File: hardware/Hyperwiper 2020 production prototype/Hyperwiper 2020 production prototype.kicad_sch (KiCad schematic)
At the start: 28 parts, among them J1 Conn_01x05, K1 Main Power relay, K2 Wiper control relay, Q1 PN2222A, Q2 IRF540N, SW1 ON-OFF, SW2 SW_Reed, U1 Teensy4.0, U3 Voltage regulator

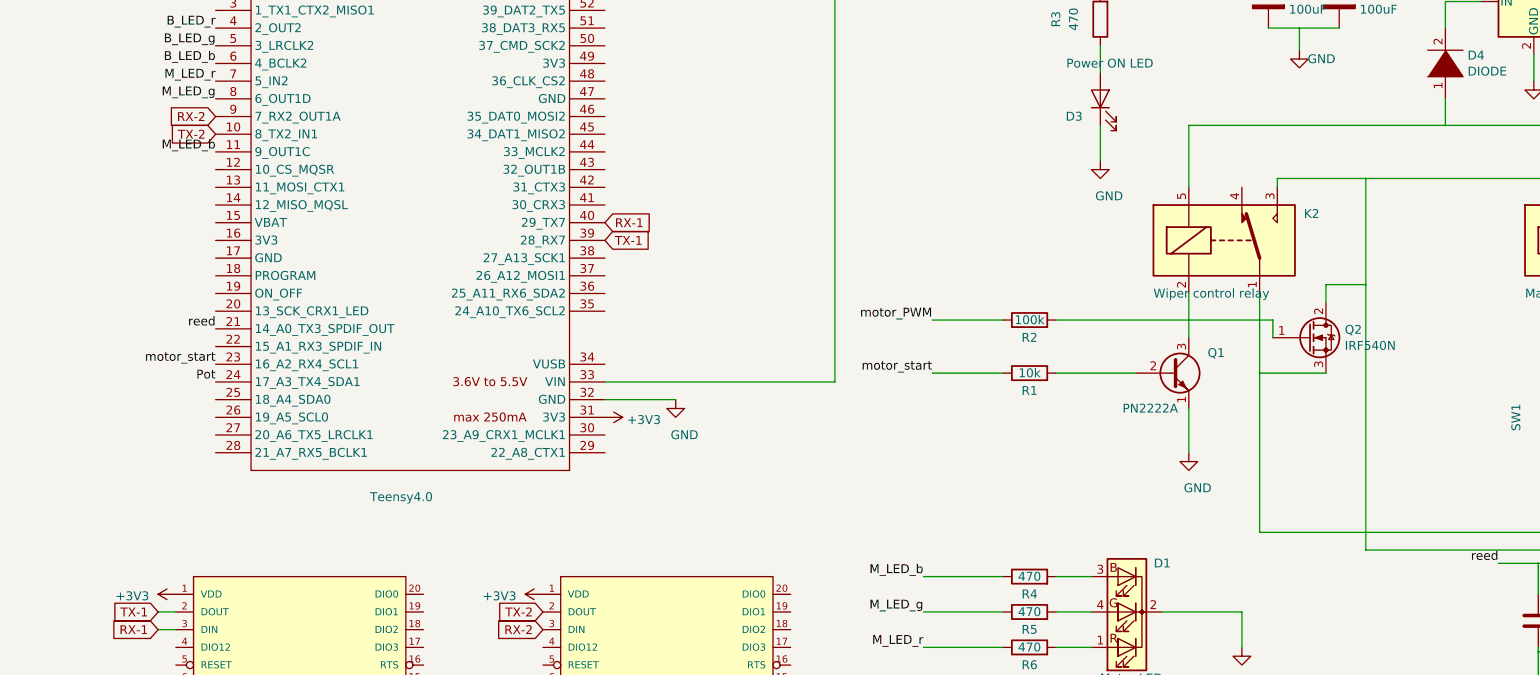
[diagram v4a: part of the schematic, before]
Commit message: Updated schematic for MOSFET
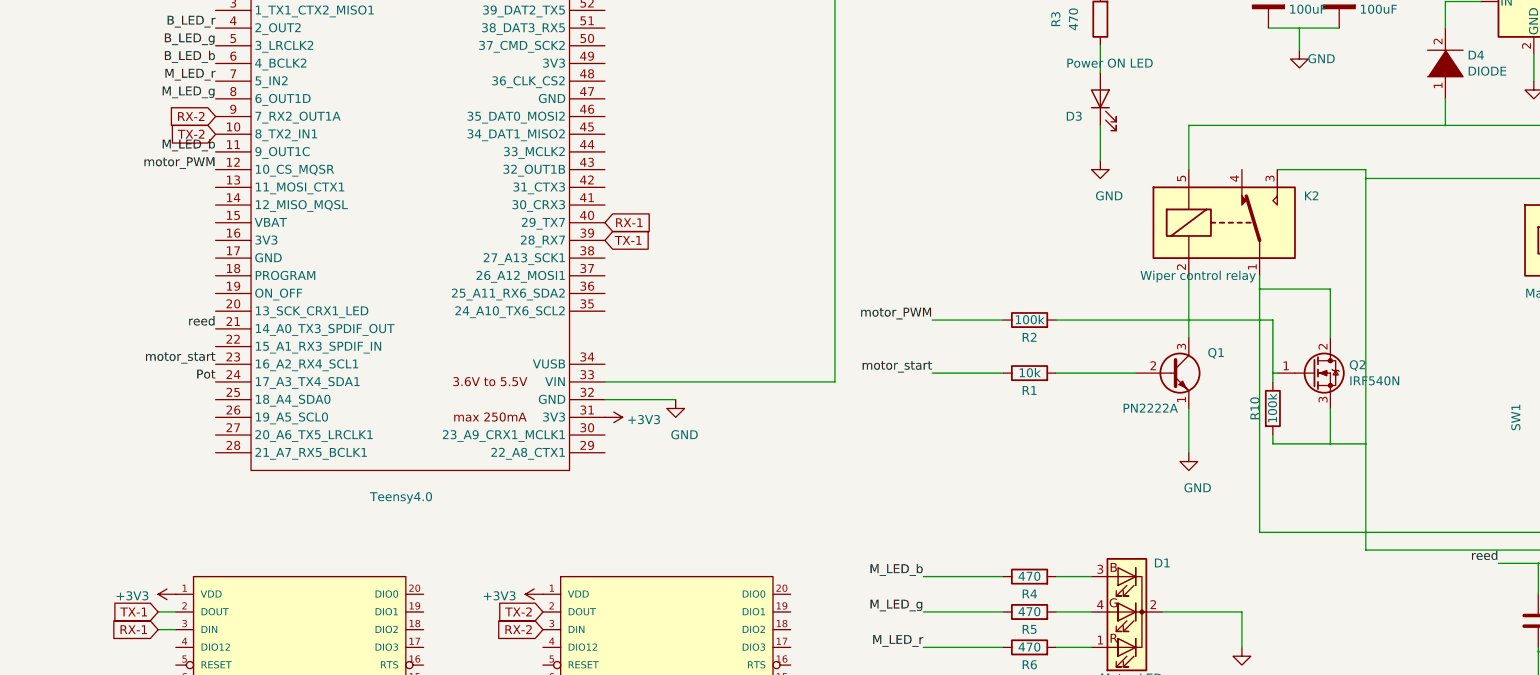
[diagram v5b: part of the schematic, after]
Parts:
- added R10: 100k, Resistor_THT:R_Axial_DIN0207_L6.3mm_D2.5mm_P10.16mm_Horizontal, symbol Device:R
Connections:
- net motor_PWM: now also U1.12 (10_CS_MQSR)
- net at Q2.1 (G), R2.2: now also R10.1
- net at J1.1 (Pin_1), K1.1, K1.5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: now also Q2.2 (D); no longer Q2.3 (S)
- net at J1.2 (Pin_2), K1.4, K2.3: now also Q2.3 (S), R10.2; no longer Q2.2 (D)
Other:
- moved on the sheet: K2, Q2
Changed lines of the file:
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@@
   )
   (junction (at 179.07 20.32) (diameter 0.259) (color 0 0 0 0))
-  (junction (at 201.93 82.55) (diameter 0.259) (color 0 0 0 0))
+  (junction (at 201.93 70.485) (diameter 0.259) (color 0 0 0 0))
+  (junction (at 203.835 82.55) (diameter 0.259) (color 0 0 0 0))
   (junction (at 207.645 33.02) (diameter 0.259) (color 0 0 0 0))
+  (junction (at 212.09 92.71) (diameter 0.259) (color 0 0 0 0))
   (junction (at 213.36 20.32) (diameter 0.259) (color 0 0 0 0))
   (junction (at 217.17 54.61) (diameter 0.259) (color 0 0 0 0))
-  (junction (at 217.17 69.85) (diameter 0.259) (color 0 0 0 0))
+  (junction (at 217.17 92.71) (diameter 0.259) (color 0 0 0 0))
   (junction (at 228.6 46.99) (diameter 0.259) (color 0 0 0 0))
   (junction (at 241.935 109.855) (diameter 0.259) (color 0 0 0 0))
@@
     (stroke (width 0) (type solid) (color 0 0 0 0))
   )
-  (wire (pts (xy 191.77 55.88) (xy 191.77 46.99))
-    (stroke (width 0) (type solid) (color 0 0 0 0))
-  )
-  (wire (pts (xy 191.77 71.12) (xy 191.77 77.47))
+  (wire (pts (xy 191.77 53.34) (xy 191.77 46.99))
+    (stroke (width 0) (type solid) (color 0 0 0 0))
+  )
+  (wire (pts (xy 191.77 68.58) (xy 191.77 77.47))
     (stroke (width 0) (type solid) (color 0 0 0 0))
   )
@@
     (stroke (width 0) (type solid) (color 0 0 0 0))
   )
-  (wire (pts (xy 201.93 71.12) (xy 201.93 82.55))
-    (stroke (width 0) (type solid) (color 0 0 0 0))
-  )
-  (wire (pts (xy 201.93 82.55) (xy 201.93 105.41))
-    (stroke (width 0) (type solid) (color 0 0 0 0))
-  )
-  (wire (pts (xy 201.93 82.55) (xy 211.455 82.55))
+  (wire (pts (xy 201.93 68.58) (xy 201.93 70.485))
+    (stroke (width 0) (type solid) (color 0 0 0 0))
+  )
+  (wire (pts (xy 201.93 70.485) (xy 201.93 105.41))
+    (stroke (width 0) (type solid) (color 0 0 0 0))
+  )
+  (wire (pts (xy 201.93 70.485) (xy 212.09 70.485))
     (stroke (width 0) (type solid) (color 0 0 0 0))
   )
@@
     (stroke (width 0) (type solid) (color 0 0 0 0))
   )
-  (wire (pts (xy 203.835 74.93) (xy 203.835 77.47))
-    (stroke (width 0) (type solid) (color 0 0 0 0))
-  )
-  (wire (pts (xy 204.47 54.61) (xy 217.17 54.61))
-    (stroke (width 0) (type solid) (color 0 0 0 0))
-  )
-  (wire (pts (xy 204.47 55.88) (xy 204.47 54.61))
+  (wire (pts (xy 203.835 74.93) (xy 203.835 82.55))
+    (stroke (width 0) (type solid) (color 0 0 0 0))
+  )
+  (wire (pts (xy 203.835 82.55) (xy 204.47 82.55))
+    (stroke (width 0) (type solid) (color 0 0 0 0))
+  )
+  (wire (pts (xy 203.835 83.82) (xy 203.835 82.55))
+    (stroke (width 0) (type solid) (color 0 0 0 0))
+  )
+  (wire (pts (xy 203.835 92.71) (xy 203.835 91.44))
+    (stroke (width 0) (type solid) (color 0 0 0 0))
+  )
+  (wire (pts (xy 203.835 92.71) (xy 212.09 92.71))
+    (stroke (width 0) (type solid) (color 0 0 0 0))
+  )
+  (wire (pts (xy 204.47 53.34) (xy 217.17 53.34))
     (stroke (width 0) (type solid) (color 0 0 0 0))
   )
@@
     (stroke (width 0) (type solid) (color 0 0 0 0))
   )
-  (wire (pts (xy 211.455 69.85) (xy 217.17 69.85))
-    (stroke (width 0) (type solid) (color 0 0 0 0))
-  )
-  (wire (pts (xy 211.455 72.39) (xy 211.455 69.85))
+  (wire (pts (xy 212.09 70.485) (xy 212.09 77.47))
+    (stroke (width 0) (type solid) (color 0 0 0 0))
+  )
+  (wire (pts (xy 212.09 87.63) (xy 212.09 92.71))
+    (stroke (width 0) (type solid) (color 0 0 0 0))
+  )
+  (wire (pts (xy 212.09 92.71) (xy 217.17 92.71))
     (stroke (width 0) (type solid) (color 0 0 0 0))
   )
@@
     (stroke (width 0) (type solid) (color 0 0 0 0))
   )
-  (wire (pts (xy 217.17 54.61) (xy 217.17 69.85))
+  (wire (pts (xy 217.17 54.61) (xy 217.17 53.34))
+    (stroke (width 0) (type solid) (color 0 0 0 0))
+  )
+  (wire (pts (xy 217.17 54.61) (xy 217.17 92.71))
     (stroke (width 0) (type solid) (color 0 0 0 0))
   )
@@
     (stroke (width 0) (type solid) (color 0 0 0 0))
   )
-  (wire (pts (xy 217.17 69.85) (xy 217.17 107.95))
+  (wire (pts (xy 217.17 92.71) (xy 217.17 107.95))
     (stroke (width 0) (type solid) (color 0 0 0 0))
   )
@@
   )
   (label "M_LED_b" (at 52.07 50.8 180)
+    (effects (font (size 1.27 1.27)) (justify right bottom))
+  )
+  (label "motor_PWM" (at 52.07 53.34 180)
     (effects (font (size 1.27 1.27)) (justify right bottom))
   )
@@
     (pin "2")
   )
+  (symbol (lib_id "Device:R") (at 203.835 87.63 0) (unit 1)
+    (in_bom yes) (on_board yes)
+    (property "Reference" "R10" (id 0) (at 201.295 87.63 90))
+    (property "Value" "100k" (id 1) (at 203.835 87.63 90))
+    (property "Footprint" "Resistor_THT:R_Axial_DIN0207_L6.3mm_D2.5mm_P10.16mm_Horizontal" (id 2) (at 202.057 87.63 90)
+      (effects (font (size 1.27 1.27)) hide)
+    )
+    (property "Datasheet" "~" (id 3) (at 203.835 87.63 0)
+      (effects (font (size 1.27 1.27)) hide)
+    )
+    (pin "1")
+    (pin "2")
+  )
   (symbol (lib_id "Device:LED") (at 179.07 43.18 90) (unit 1)
     (in_bom yes) (on_board yes)
@@
     (pin "3")
   )
-  (symbol (lib_id "Transistor_FET:IRF540N") (at 208.915 77.47 0) (unit 1)
-    (in_bom yes) (on_board yes)
-    (property "Reference" "Q2" (id 0) (at 214.1475 76.3206 0)
-      (effects (font (size 1.27 1.27)) (justify left))
-    )
-    (property "Value" "IRF540N" (id 1) (at 214.1475 78.6193 0)
-      (effects (font (size 1.27 1.27)) (justify left))
-    )
-    (property "Footprint" "Package_TO_SOT_THT:TO-220-3_Vertical" (id 2) (at 215.265 79.375 0)
+  (symbol (lib_id "Transistor_FET:IRF540N") (at 209.55 82.55 0) (unit 1)
+    (in_bom yes) (on_board yes)
+    (property "Reference" "Q2" (id 0) (at 214.7825 81.4006 0)
+      (effects (font (size 1.27 1.27)) (justify left))
+    )
+    (property "Value" "IRF540N" (id 1) (at 214.7825 83.6993 0)
+      (effects (font (size 1.27 1.27)) (justify left))
+    )
+    (property "Footprint" "Package_TO_SOT_THT:TO-220-3_Vertical" (id 2) (at 215.9 84.455 0)
       (effects (font (size 1.27 1.27) italic) (justify left) hide)
     )
-    (property "Datasheet" "http://www.irf.com/product-info/datasheets/data/irf540n.pdf" (id 3) (at 208.915 77.47 0)
+    (property "Datasheet" "http://www.irf.com/product-info/datasheets/data/irf540n.pdf" (id 3) (at 209.55 82.55 0)
       (effects (font (size 1.27 1.27)) (justify left) hide)
     )
@@
     (pin "4")
   )
-  (symbol (lib_id "Relay:SANYOU_SRD_Form_C") (at 196.85 63.5 0) (unit 1)
-    (in_bom yes) (on_board yes)
-    (property "Reference" "K2" (id 0) (at 208.28 59.69 0)
-      (effects (font (size 1.27 1.27)) (justify left))
-    )
-    (property "Value" "Wiper control relay" (id 1) (at 186.69 71.12 0)
-      (effects (font (size 1.27 1.27)) (justify left))
-    )
-    (property "Footprint" "Relay_THT:Relay_SPDT_SANYOU_SRD_Series_Form_C" (id 2) (at 208.28 64.77 0)
+  (symbol (lib_id "Relay:SANYOU_SRD_Form_C") (at 196.85 60.96 0) (unit 1)
+    (in_bom yes) (on_board yes)
+    (property "Reference" "K2" (id 0) (at 208.28 57.15 0)
+      (effects (font (size 1.27 1.27)) (justify left))
+    )
+    (property "Value" "Wiper control relay" (id 1) (at 184.785 68.58 0)
+      (effects (font (size 1.27 1.27)) (justify left))
+    )
+    (property "Footprint" "Relay_THT:Relay_SPDT_SANYOU_SRD_Series_Form_C" (id 2) (at 208.28 62.23 0)
       (effects (font (size 1.27 1.27)) (justify left) hide)
     )
-    (property "Datasheet" "http://www.sanyourelay.ca/public/products/pdf/SRD.pdf" (id 3) (at 196.85 63.5 0)
+    (property "Datasheet" "http://www.sanyourelay.ca/public/products/pdf/SRD.pdf" (id 3) (at 196.85 60.96 0)
       (effects (font (size 1.27 1.27)) hide)
     )
@@
       (reference "R9") (unit 1) (value "470") (footprint "Resistor_THT:R_Axial_DIN0207_L6.3mm_D2.5mm_P10.16mm_Horizontal")
     )
+    (path "/262574bc-5200-41bf-819f-e4ebc4aa93eb"
+      (reference "R10") (unit 1) (value "100k") (footprint "Resistor_THT:R_Axial_DIN0207_L6.3mm_D2.5mm_P10.16mm_Horizontal")
+    )
     (path "/3c75595d-bef3-4439-a823-4b03a4737025"
